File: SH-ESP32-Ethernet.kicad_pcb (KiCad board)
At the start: 4 copper layers, 23.5 x 55.5 mm, 39 parts, among them J301 RJ45__HY931147C_MAG_LED_POE, J302 GPIO, J303 Conn_01x03, U301 LAN8720A, X301 50Mhz

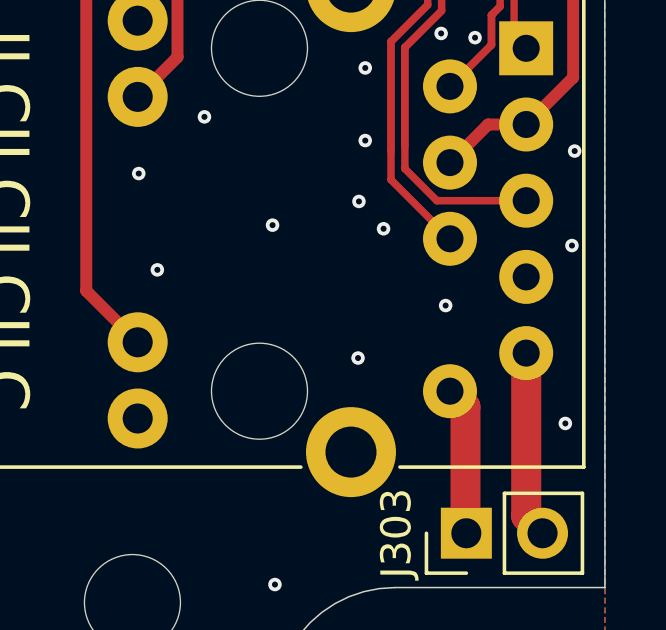
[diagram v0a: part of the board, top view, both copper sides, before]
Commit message: Finalise for Production - LCSC Part numbers - Fix Jack footprint for missing Pad - Sheet names
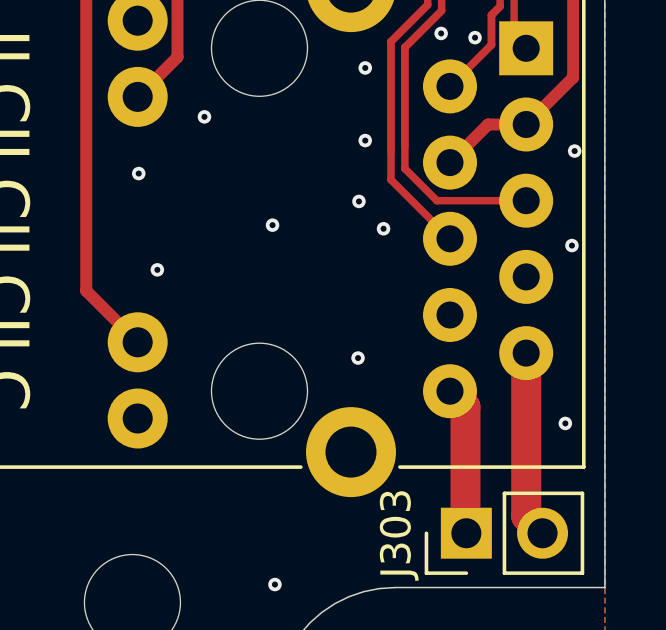
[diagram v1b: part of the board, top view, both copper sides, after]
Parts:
- J301: footprint Connector_RJ:RJ45_Abracon_ARJP11A-MA_Horizontal -> SH-ESP32-Ethernet:RJ45_HANRUN-HY931147C-Horizontal
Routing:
- net GND: vias 73 -> 72

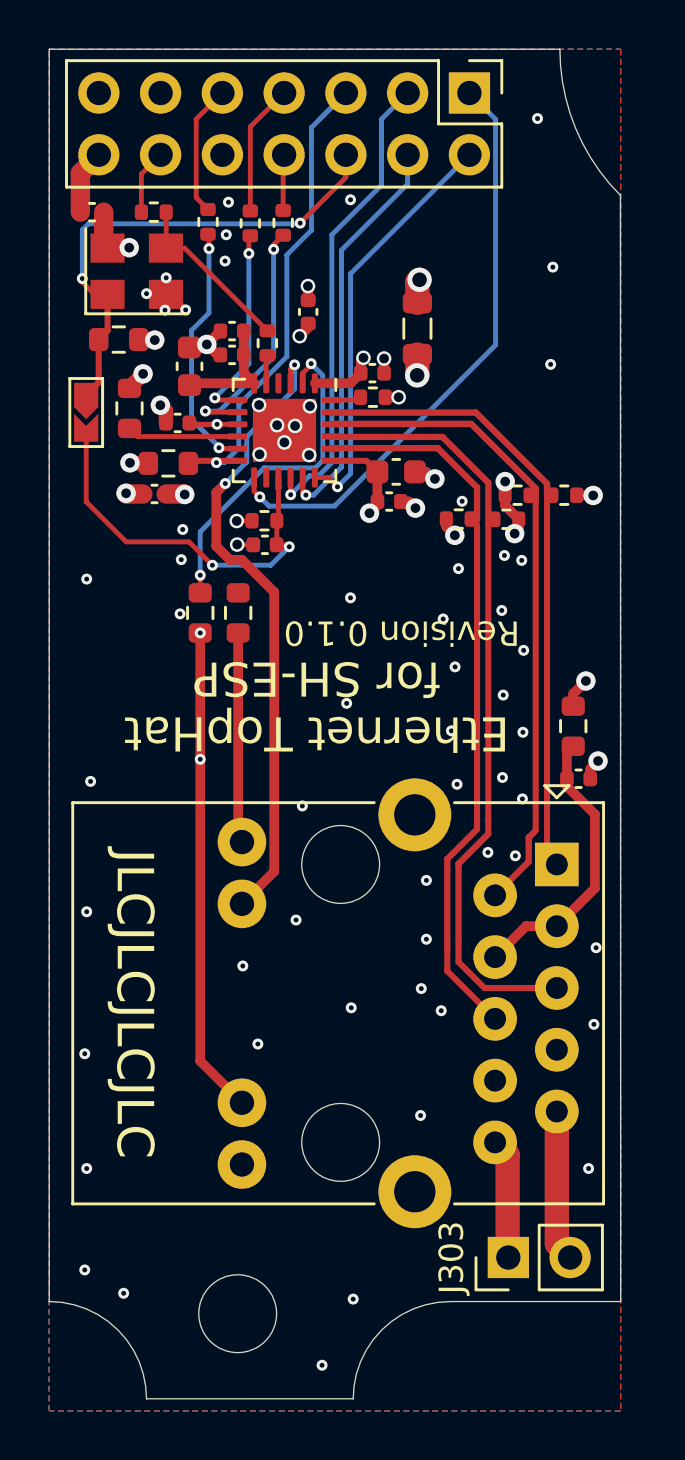
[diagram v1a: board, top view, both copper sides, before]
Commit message: Update for SH-ESP R0.3 Header & Mounting Hole Positions
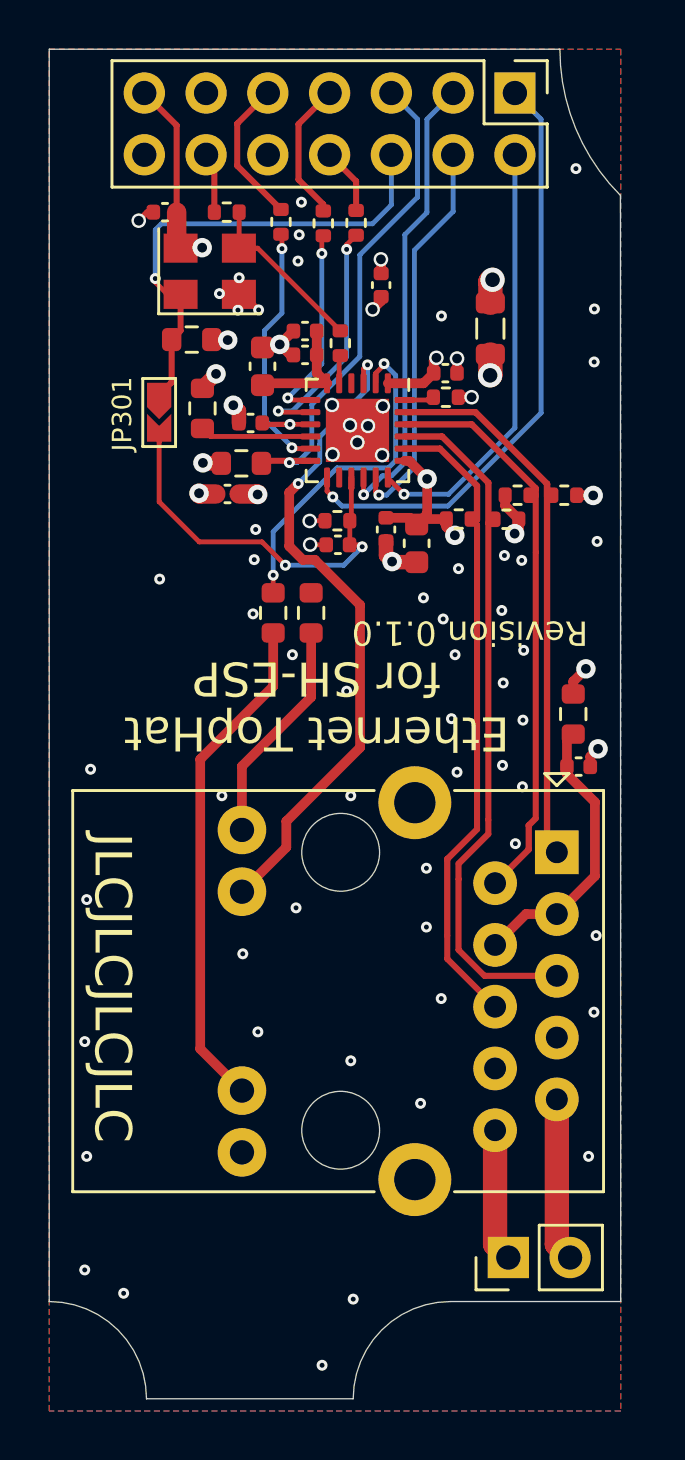
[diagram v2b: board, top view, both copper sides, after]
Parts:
- H1002: footprint SH-ESP32:MountingHole_3.2mm_M3_Unplated -> SH-ESP32-Ethernet:MountingSlot_3.2mm_M3_Unplated
- moved C1002 3.20 mm to (162.2, 66.7)
- moved C304 3.06 mm to (163.6, 77.3), turned to 90 degrees
- moved C1001 3.00 mm to (156.8, 72.4)
- moved C1003 3.00 mm to (155.8, 75.3)
- moved C1004 3.00 mm to (153.3, 63.7)
- moved C301 3.00 mm to (159.0, 68.6)
- moved C302 3.00 mm to (159.0, 69.6)
- moved C303 3.00 mm to (157.3, 70.0)
- moved C305 3.00 mm to (164.8, 70.3)
- moved C306 3.00 mm to (160.4, 77.4)
- moved FB301 3.00 mm to (166.6, 68.5)
- moved JP301 3.00 mm to (153.0, 71.9)
- moved R301 3.00 mm to (156.4, 74.0)
- moved R302 3.00 mm to (154.8, 71.8)
- moved R303 3.00 mm to (154.4, 68.9)
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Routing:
- net +3V3: track 10.2 -> 15.7 mm
- net /IOHeader/TX-: track 30.3 -> 26.8 mm
- net /IOHeader/RX-: track 27.2 -> 23.7 mm
- net /IOHeader/TX+: track 32.2 -> 28.7 mm
- net /IOHeader/RX+: track 26.7 -> 23.2 mm
- net GND: track 15.4 -> 13.8 mm, vias 72 -> 71
- net VDDA: track 12.7 -> 14.3 mm
- net /IOHeader/PHY_CLK: track 3.83 -> 2.50 mm
- net /IOHeader/LED_Y_CA: track 26.2 -> 27.3 mm
- net /IOHeader/PHY_MDIO: track 22.1 -> 21.0 mm
- net /IOHeader/PHY_RESET_N: track 21.1 -> 20.1 mm, vias 2 -> 1
- net /IOHeader/RMII_TXD1: track 17.0 -> 17.9 mm
- net /IOHeader/LED_Y_AN: track 8.66 -> 9.50 mm
- net /IOHeader/LED_R_AN: track 20.0 -> 20.8 mm, vias 2 -> 0
- net /IOHeader/RMI_CRS_DV: track 5.44 -> 6.06 mm
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
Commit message: Updates for missing resistor / route on Clock line - Created some major re-routing / tidy up
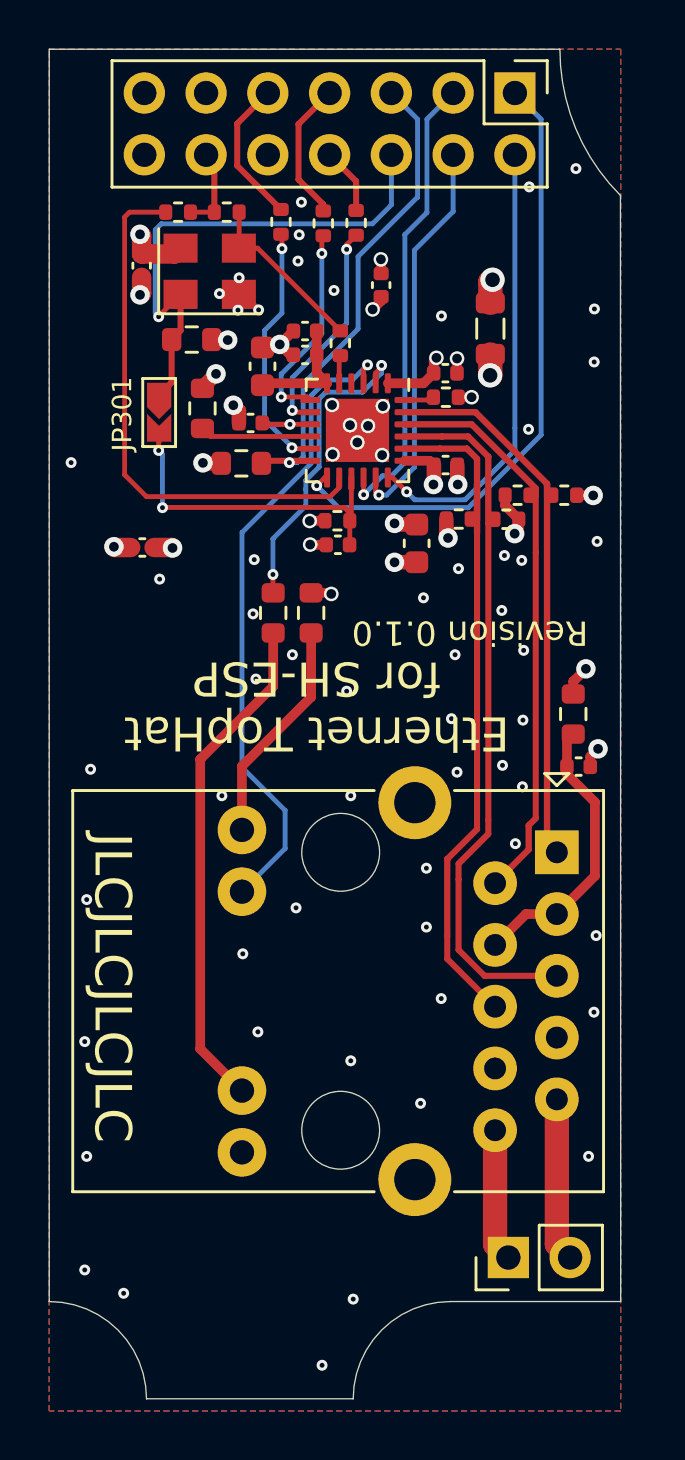
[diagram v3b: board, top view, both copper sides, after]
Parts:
- added R318: 33R, Resistor_SMD:R_0402_1005Metric, F.Cu at (153.8, 63.7)
- moved C1003 4.13 mm to (152.3, 77.5)
- moved C307 3.61 mm to (164.8, 74.1), turned to 180 degrees
- moved C1004 2.40 mm to (152.3, 65.9), turned to 90 degrees
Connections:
- U301 pad 14: (no net) -> Net-(R318-Pad1)
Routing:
- net Net-(R318-Pad1): track 0.00 -> 22.1 mm
- net +3V3: track 15.7 -> 10.5 mm
- net VDDA: track 14.3 -> 11.3 mm, vias 8 -> 9
- net /IOHeader/TX-: track 26.8 -> 29.4 mm
- net /IOHeader/nRST: track 17.0 -> 15.2 mm
- net /IOHeader/PHY_RESET_N: track 20.1 -> 21.6 mm
- net Net-(R304-Pad1): track 10.2 -> 9.07 mm
- net /IOHeader/PHY_MDC: track 24.8 -> 25.9 mm
- net /IOHeader/PHY_CLK: track 2.50 -> 3.48 mm
- net /IOHeader/nINTSEL-LED2: track 13.9 -> 12.9 mm
- net /IOHeader/RMII_TXD1: track 17.9 -> 18.6 mm
- net /IOHeader/TX+: track 28.7 -> 29.4 mm
- net /IOHeader/LED_Y_CA: track 27.3 -> 26.7 mm, vias 2 -> 1
- net GND: track 13.8 -> 14.4 mm, vias 71 -> 75
